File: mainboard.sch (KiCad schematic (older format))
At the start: 10 parts, among them J1 105017-1001, J2 XT60-M, U1 ESP32-WROOM-32E_(16MB), U2 CH340E, U3 AMS1117-3.3

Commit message: update
toevoegen mosfet en versterker in schematic
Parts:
- added C3, C4, C5, C6, C7, C8, C9: C, Capacitor_SMD:C_0805_2012Metric_Pad1.18x1.45mm_HandSolder, symbol Device:C
- added D1: D, Diode_SMD:D_0402_1005Metric_Pad0.77x0.64mm_HandSolder, symbol Device:D
- added Q1, Q2: AOD4184A, mylibs:DPAK228P994X240-4N, symbol AOD4184A:AOD4184A
- added R2, R3, R4, R5, R6: R, Resistor_SMD:R_0805_2012Metric_Pad1.20x1.40mm_HandSolder, symbol Device:R
- added U4: PAM8403DR, mylibs:SOIC127P605X150-16N, symbol PAM8403DR:PAM8403DR
- J1: symbol 105017-1001:105017-1001 -> mainboard-rescue:105017-1001-105017-1001
- J2: symbol XT60-M:XT60-M -> mainboard-rescue:XT60-M-XT60-M
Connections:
- net labels added: +OUT_L, +OUT_R, -OUT_L, -OUT_R, 5V, INL, INR, Mosfet_Out-, Mosfet_Trig, SHND, mute
- wire segments 20 -> 57
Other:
- note added: "High-Power-Mosfet\n"
- note added: "Programmer"
- note added: "Versterker-PAM8403 XH-M179\n"
- note added: "Voeding\n"
- moved on the sheet: C1, C2, R1, S1, S2, U1, U2, U3

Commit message: ik heb ervoor gezorgd dat de schakeling geen vuurwerk meer is
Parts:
- Q1, Q2: symbol AOD4184A:AOD4184A -> mainboard-rescue:AOD4184A-AOD4184A
- U4: symbol PAM8403DR:PAM8403DR -> mainboard-rescue:PAM8403DR-PAM8403DR
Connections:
- wire segments 57 -> 56
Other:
- moved on the sheet: C6
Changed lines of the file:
@@
 $EndComp
 $Comp
-L AOD4184A:AOD4184A Q1
+L mainboard-rescue:AOD4184A-AOD4184A Q1
 U 1 1 60421934
 P 9150 2900
@@
 	9700 3000 9700 3350
 $Comp
-L AOD4184A:AOD4184A Q2
+L mainboard-rescue:AOD4184A-AOD4184A Q2
 U 1 1 60422823
 P 9800 2900
@@
 L Device:C C6
 U 1 1 60534571
-P 4050 6100
-F 0 "C6" V 3798 6100 50  0000 C CNN
-F 1 "C" V 3889 6100 50  0000 C CNN
-F 2 "Capacitor_SMD:C_0805_2012Metric_Pad1.18x1.45mm_HandSolder" H 4088 5950 50  0001 C CNN
-F 3 "~" H 4050 6100 50  0001 C CNN
-	1    4050 6100
+P 4350 6100
+F 0 "C6" V 4098 6100 50  0000 C CNN
+F 1 "C" V 4189 6100 50  0000 C CNN
+F 2 "Capacitor_SMD:C_0805_2012Metric_Pad1.18x1.45mm_HandSolder" H 4388 5950 50  0001 C CNN
+F 3 "~" H 4350 6100 50  0001 C CNN
+	1    4350 6100
 	0    1    1    0
-$EndComp
-$Comp
-L power:GND #PWR0112
-U 1 1 605351B6
-P 4400 6100
-F 0 "#PWR0112" H 4400 5850 50  0001 C CNN
-F 1 "GND" V 4405 5972 50  0000 R CNN
-F 2 "" H 4400 6100 50  0001 C CNN
-F 3 "" H 4400 6100 50  0001 C CNN
-	1    4400 6100
-	0    -1   -1   0
 $EndComp
 Wire Notes Line
@@
 Versterker-PAM8403 XH-M179\n
 $Comp
-L PAM8403DR:PAM8403DR U4
+L mainboard-rescue:PAM8403DR-PAM8403DR U4
 U 1 1 60500031
 P 3300 6700
@@
 Text GLabel 1600 7400 3    50   Input ~ 0
 INL
-Wire Wire Line
-	4200 6100 4300 6100
 Text GLabel 4950 6200 2    50   Input ~ 0
 5V
 Wire Wire Line
-	4450 5950 4300 5950
-Wire Wire Line
-	4300 5950 4300 6100
-Connection ~ 4300 6100
-Wire Wire Line
-	4300 6100 4400 6100
-Wire Wire Line
 	4950 6200 4950 6300
-Text GLabel 4450 5950 2    50   Input ~ 0
-5V
 $Comp
 L power:GND #PWR0110
@@
 	1    0    0    -1
 $EndComp
+Text GLabel 4050 6000 1    50   Input ~ 0
+5V
+Wire Wire Line
+	3900 6100 4050 6100
+Wire Wire Line
+	4050 6100 4050 6000
+Connection ~ 4050 6100
+Wire Wire Line
+	4050 6100 4200 6100
+$Comp
+L power:GND #PWR?
+U 1 1 60477405
+P 4500 6100
+F 0 "#PWR?" H 4500 5850 50  0001 C CNN
+F 1 "GND" V 4505 5972 50  0000 R CNN
+F 2 "" H 4500 6100 50  0001 C CNN
+F 3 "" H 4500 6100 50  0001 C CNN
+	1    4500 6100
+	0    -1   -1   0
+$EndComp
 $EndSCHEMATC

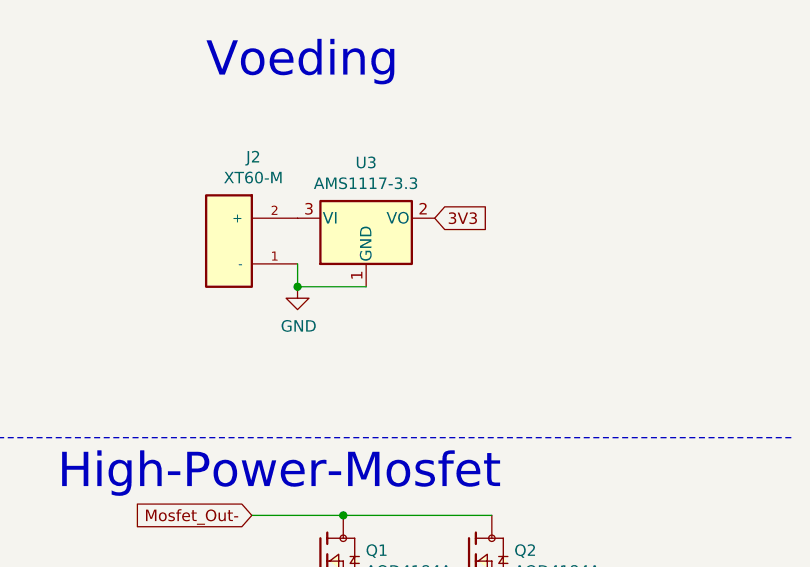
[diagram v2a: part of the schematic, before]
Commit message: condensator toegevoegd aan ldo
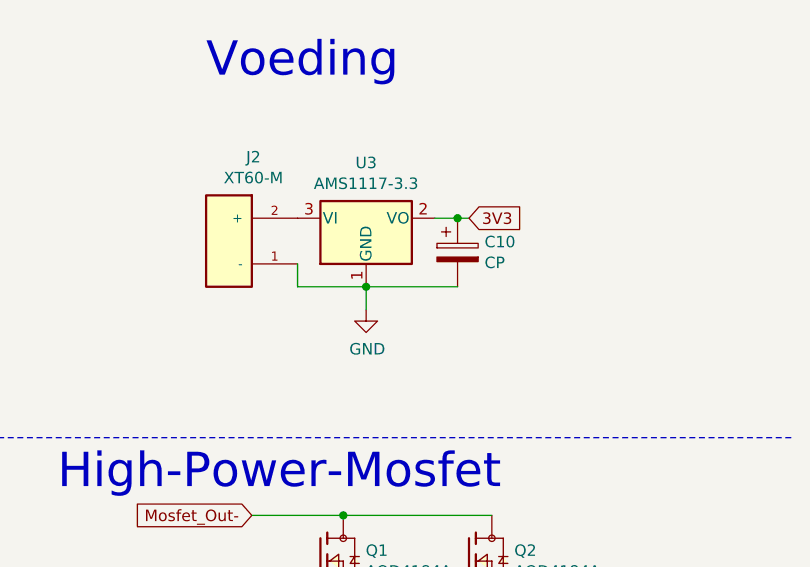
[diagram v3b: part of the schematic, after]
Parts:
- added C10: CP, Capacitor_Tantalum_SMD:CP_EIA-1608-08_AVX-J_Pad1.25x1.05mm_HandSolder, symbol Device:CP
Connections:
- wire segments 56 -> 60
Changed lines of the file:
@@
 Wire Wire Line
 	9250 2700 9900 2700
-Text GLabel 9650 1400 2    50   Input ~ 0
+Text GLabel 9800 1400 2    50   Input ~ 0
 3V3
-Connection ~ 9050 1700
 $Comp
 L power:GND #PWR01
 U 1 1 6046FD41
-P 9050 1700
-F 0 "#PWR01" H 9050 1450 50  0001 C CNN
-F 1 "GND" H 9055 1527 50  0000 C CNN
-F 2 "" H 9050 1700 50  0001 C CNN
-F 3 "" H 9050 1700 50  0001 C CNN
-	1    9050 1700
-	1    0    0    -1
-$EndComp
-Wire Wire Line
-	9050 1700 9050 1600
-Wire Wire Line
-	9350 1700 9050 1700
+P 9350 1800
+F 0 "#PWR01" H 9350 1550 50  0001 C CNN
+F 1 "GND" H 9355 1627 50  0000 C CNN
+F 2 "" H 9350 1800 50  0001 C CNN
+F 3 "" H 9350 1800 50  0001 C CNN
+	1    9350 1800
+	1    0    0    -1
+$EndComp
+Wire Wire Line
+	9350 1700 9350 1800
 $Comp
 L mainboard-rescue:XT60-M-XT60-M J2
@@
 	1    8750 1500
 	-1   0    0    1
-$EndComp
-$Comp
-L Regulator_Linear:AMS1117-3.3 U3
-U 1 1 60450E15
-P 9350 1400
-F 0 "U3" H 9350 1642 50  0000 C CNN
-F 1 "AMS1117-3.3" H 9350 1551 50  0000 C CNN
-F 2 "Package_TO_SOT_SMD:SOT-223-3_TabPin2" H 9350 1600 50  0001 C CNN
-F 3 "http://www.advanced-monolithic.com/pdf/ds1117.pdf" H 9450 1150 50  0001 C CNN
-	1    9350 1400
-	1    0    0    -1
 $EndComp
 Text GLabel 1900 1450 1    50   Input ~ 0
@@
 	4050 6100 4200 6100
 $Comp
-L power:GND #PWR?
+L power:GND #PWR04
 U 1 1 60477405
 P 4500 6100
-F 0 "#PWR?" H 4500 5850 50  0001 C CNN
+F 0 "#PWR04" H 4500 5850 50  0001 C CNN
 F 1 "GND" V 4505 5972 50  0000 R CNN
 F 2 "" H 4500 6100 50  0001 C CNN
@@
 	0    -1   -1   0
 $EndComp
+Wire Wire Line
+	9650 1400 9750 1400
+$Comp
+L Regulator_Linear:AMS1117-3.3 U3
+U 1 1 60450E15
+P 9350 1400
+F 0 "U3" H 9350 1642 50  0000 C CNN
+F 1 "AMS1117-3.3" H 9350 1551 50  0000 C CNN
+F 2 "Package_TO_SOT_SMD:SOT-223-3_TabPin2" H 9350 1600 50  0001 C CNN
+F 3 "http://www.advanced-monolithic.com/pdf/ds1117.pdf" H 9450 1150 50  0001 C CNN
+	1    9350 1400
+	1    0    0    -1
+$EndComp
+Wire Wire Line
+	9050 1600 9050 1700
+Wire Wire Line
+	9050 1700 9350 1700
+Connection ~ 9350 1700
+$Comp
+L Device:CP C10
+U 1 1 60484A4F
+P 9750 1550
+F 0 "C10" H 9868 1596 50  0000 L CNN
+F 1 "CP" H 9868 1505 50  0000 L CNN
+F 2 "Capacitor_Tantalum_SMD:CP_EIA-1608-08_AVX-J_Pad1.25x1.05mm_HandSolder" H 9788 1400 50  0001 C CNN
+F 3 "~" H 9750 1550 50  0001 C CNN
+	1    9750 1550
+	1    0    0    -1
+$EndComp
+Connection ~ 9750 1400
+Wire Wire Line
+	9750 1400 9800 1400
+Wire Wire Line
+	9750 1700 9350 1700
 $EndSCHEMATC

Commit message: ordenen pcb
kheb wa plek vrijgelaten voor de io pinnen
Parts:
- removed C2: C, Capacitor_SMD:C_0805_2012Metric_Pad1.18x1.45mm_HandSolder, symbol Device:C
- removed D1: D, Diode_SMD:D_0402_1005Metric_Pad0.77x0.64mm_HandSolder, symbol Device:D
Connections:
- wire segments 60 -> 57
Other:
- note added: "PWM\n"
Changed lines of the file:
@@
 	8850 5450 8850 5600
 Wire Wire Line
-	9100 5350 9100 4700
-Wire Wire Line
-	9100 4700 9550 4700
-Connection ~ 9550 4700
-Wire Wire Line
-	9550 4700 9650 4700
-Wire Wire Line
 	9650 4700 9650 5000
 Wire Wire Line
 	8850 5600 9250 5600
-$Comp
-L Device:C C2
-U 1 1 60436DBE
-P 9550 4850
-F 0 "C2" H 9665 4896 50  0000 L CNN
-F 1 "C" H 9665 4805 50  0000 L CNN
-F 2 "Capacitor_SMD:C_0805_2012Metric_Pad1.18x1.45mm_HandSolder" H 9588 4700 50  0001 C CNN
-F 3 "~" H 9550 4850 50  0001 C CNN
-	1    9550 4850
-	1    0    0    -1
-$EndComp
 $Comp
 L power:GND #PWR0103
@@
 Wire Wire Line
 	9250 5550 9250 5500
-Wire Wire Line
-	8350 5350 9100 5350
 NoConn ~ 10050 5500
 NoConn ~ 10050 6000
@@
 $EndComp
 $Comp
-L Device:D D1
-U 1 1 60426053
-P 9250 3900
-F 0 "D1" V 9296 3820 50  0000 R CNN
-F 1 "D" V 9205 3820 50  0000 R CNN
-F 2 "Diode_SMD:D_0402_1005Metric_Pad0.77x0.64mm_HandSolder" H 9250 3900 50  0001 C CNN
-F 3 "~" H 9250 3900 50  0001 C CNN
-	1    9250 3900
-	0    -1   -1   0
-$EndComp
-$Comp
 L Device:R R4
 U 1 1 604268D1
@@
 L power:GND #PWR0107
 U 1 1 6042DD5F
-P 9250 4050
-F 0 "#PWR0107" H 9250 3800 50  0001 C CNN
-F 1 "GND" H 9255 3877 50  0000 C CNN
-F 2 "" H 9250 4050 50  0001 C CNN
-F 3 "" H 9250 4050 50  0001 C CNN
-	1    9250 4050
+P 9250 3750
+F 0 "#PWR0107" H 9250 3500 50  0001 C CNN
+F 1 "GND" H 9255 3577 50  0000 C CNN
+F 2 "" H 9250 3750 50  0001 C CNN
+F 3 "" H 9250 3750 50  0001 C CNN
+	1    9250 3750
 	1    0    0    -1
 $EndComp
@@
 Wire Wire Line
 	9750 1700 9350 1700
+Wire Wire Line
+	9550 5000 9650 5000
+Connection ~ 9650 5000
+Text GLabel 9650 4700 2    50   Input ~ 0
+3V3
+Text GLabel 3950 1750 2    50   Input ~ 0
+3V3
+Text GLabel 3950 2050 2    50   Input ~ 0
+Mosfet_Trig
+Text Notes 3950 2650 0    50   ~ 0
+PWM\n
+Text Notes 3950 2750 0    50   ~ 0
+PWM\n
 $EndSCHEMATC

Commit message: sorry stef
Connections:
- net SHND: now also U1.14 (IO12)
- net mute: no longer names the net of U4.5 (MUTE)
- no-connect marks 4 -> 5
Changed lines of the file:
@@
 	1    0    0    -1
 $EndComp
-Text GLabel 2700 6400 0    50   Input ~ 0
-mute
 Connection ~ 4950 6650
 Wire Wire Line
@@
 Text Notes 3950 2750 0    50   ~ 0
 PWM\n
+NoConn ~ 2700 6400
+Text GLabel 3950 2350 2    50   Input ~ 0
+SHND
 $EndSCHEMATC

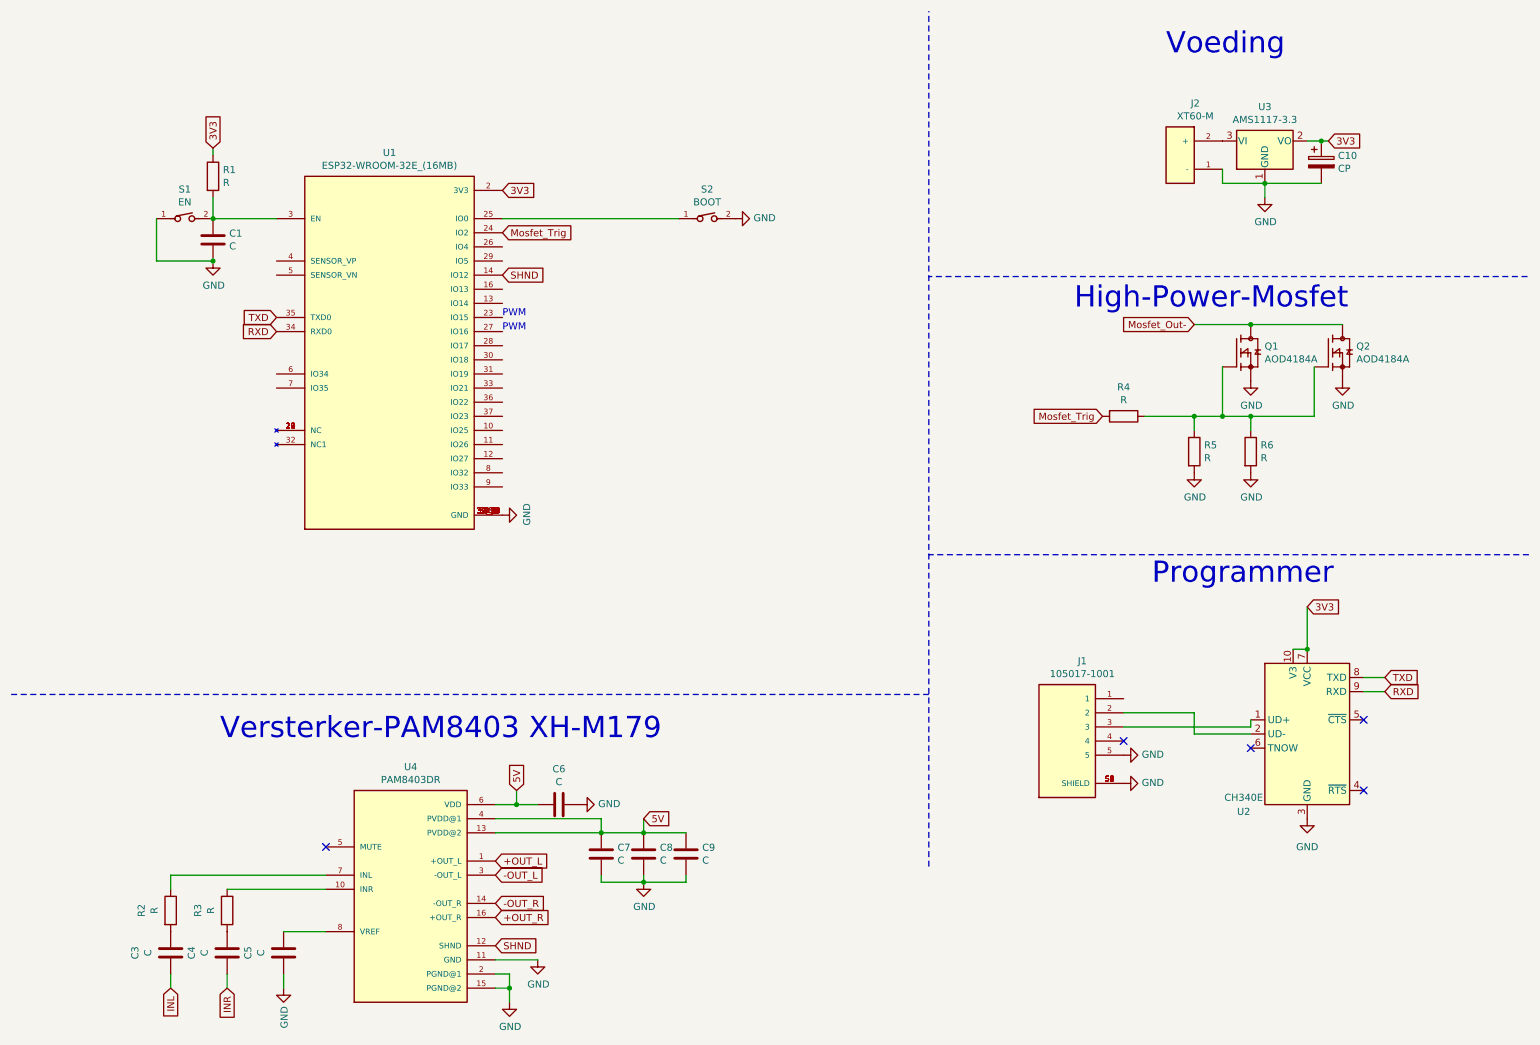
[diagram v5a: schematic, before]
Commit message: PCB herwerkt na feedback
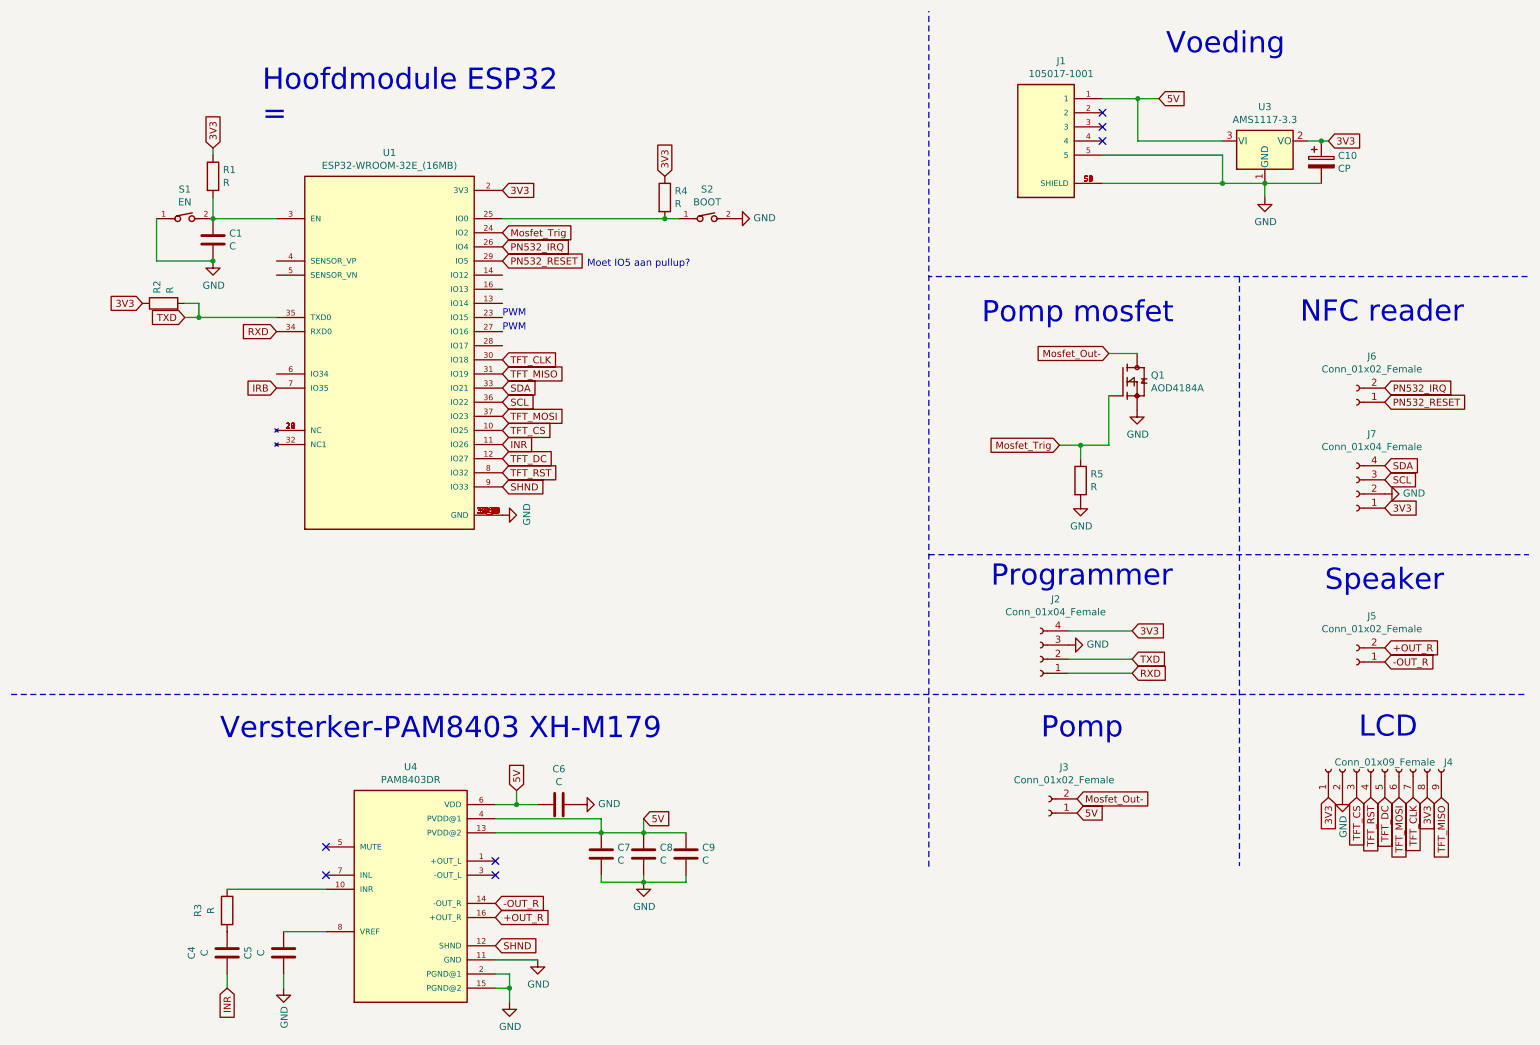
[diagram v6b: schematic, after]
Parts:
- removed C3: C, Capacitor_SMD:C_0805_2012Metric_Pad1.18x1.45mm_HandSolder, symbol Device:C
- removed J2: XT60-M, mylibs:AMASS_XT60-M, symbol mainboard-rescue:XT60-M-XT60-M
- removed Q2: AOD4184A, mylibs:DPAK228P994X240-4N, symbol mainboard-rescue:AOD4184A-AOD4184A
- removed R6: R, Resistor_SMD:R_0805_2012Metric_Pad1.20x1.40mm_HandSolder, symbol Device:R
- removed U2: CH340E, Package_SO:MSOP-10_3x3mm_P0.5mm, symbol Interface_USB:CH340E
- added J2: Conn_01x04_Female, Connector_PinSocket_2.54mm:PinSocket_1x04_P2.54mm_Vertical, symbol Connector:Conn_01x04_Female
- added J3, J5, J6: Conn_01x02_Female, Connector_PinSocket_2.54mm:PinSocket_1x02_P2.54mm_Vertical, symbol Connector:Conn_01x02_Female
- added J4: Conn_01x09_Female, Connector_PinSocket_2.54mm:PinSocket_1x09_P2.54mm_Vertical, symbol Connector:Conn_01x09_Female
- added J7: Conn_01x04_Female, symbol Connector:Conn_01x04_Female
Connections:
- net +OUT_R: now also J5.2 (Pin_2)
- net -OUT_R: now also J5.1 (Pin_1)
- net 3V3: now also R2.1, R4.1, J2.4 (Pin_4), J4.1 (Pin_1), J4.8 (Pin_8), J7.1 (Pin_1)
- net 5V: now also J1.1, U3.3 (VI), J3.1 (Pin_1)
- net GND: now also J2.3 (Pin_3), J4.2 (Pin_2), J7.2 (Pin_2)
- net INR: now also U1.11 (IO26)
- net Mosfet_Out-: now also J3.2 (Pin_2)
- net Mosfet_Trig: now also Q1.1, R5.1; no longer R4.2
- net RXD: now also J2.1 (Pin_1)
- net SHND: now also U1.9 (IO33); no longer U1.14 (IO12)
- net TXD: now also R2.2, J2.2 (Pin_2)
- net at S2.1, U1.25 (IO0): now also R4.2
- net TFT_CS: now reaches U1.10 (IO25)
- net TFT_CS: now also J4.3 (Pin_3)
- net TFT_DC: now reaches U1.12 (IO27)
- net TFT_DC: now also J4.5 (Pin_5)
- net PN532_IRQ: now reaches U1.26 (IO4)
- net PN532_IRQ: now also J6.2 (Pin_2)
- net PN532_RESET: now reaches U1.29 (IO5)
- net PN532_RESET: now also J6.1 (Pin_1)
- net TFT_CLK: now reaches U1.30 (IO18)
- net TFT_CLK: now also J4.7 (Pin_7)
- net TFT_MISO: now reaches U1.31 (IO19)
- net TFT_MISO: now also J4.9 (Pin_9)
- net SDA: now reaches U1.33 (IO21)
- net SDA: now also J7.4 (Pin_4)
- net SCL: now reaches U1.36 (IO22)
- net SCL: now also J7.3 (Pin_3)
- net TFT_MOSI: now reaches U1.37 (IO23)
- net TFT_MOSI: now also J4.6 (Pin_6)
- net IRB: now reaches U1.7 (IO35)
- net TFT_RST: now reaches U1.8 (IO32)
- net TFT_RST: now also J4.4 (Pin_4)
- net at U4.7 (INL): no longer R2.1
- net +OUT_L: no longer names the net of U4.1 (+OUT_L)
- net -OUT_L: no longer names the net of U4.3 (-OUT_L)
- no-connect marks 5 -> 7
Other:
- note added: "Hoofdmodule ESP32\n="
- note added: "LCD"
- note added: "Moet IO5 aan pullup?"
- note added: "NFC reader"
- note added: "Pomp"
- note added: "Pomp mosfet\n"
- note added: "Speaker\n"
- note removed: "High-Power-Mosfet\n"
- moved on the sheet: J1, Q1, R5

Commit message: tis fokking mooi wtf
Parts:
- removed C10: CP, Capacitor_Tantalum_SMD:CP_EIA-1608-08_AVX-J_Pad1.25x1.05mm_HandSolder, symbol Device:CP
- added C2: 100n, Capacitor_SMD:C_0805_2012Metric_Pad1.18x1.45mm_HandSolder, symbol Device:C
- added C3: 22u, Capacitor_SMD:C_0805_2012Metric_Pad1.18x1.45mm_HandSolder, symbol Device:C
- added R6, R7: 10K, Resistor_SMD:R_0805_2012Metric_Pad1.20x1.40mm_HandSolder, symbol Device:R
- C1: value C -> 100n
- C4: value C -> 0.47u
- C5: value C -> 0.1u
- C6, C7, C9: value C -> 1u
- C8: value C -> 470u
- J7: footprint (none) -> Connector_PinSocket_2.54mm:PinSocket_1x02_P2.54mm_Vertical
- R1, R2, R3, R4, R5: value R -> 10K
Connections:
- net 3V3: now also J4.9 (Pin_9), C2.2, C3.1, R6.2; no longer J4.8 (Pin_8)
- net 5V: now also C6.1; no longer C6.2
- net GND: now also C6.2, C2.1, C3.2, R7.1; no longer C6.1
- net PN532_RESET: now also R6.1
- net SHND: now also R7.2
- net TFT_CLK: now also J4.8 (Pin_8); no longer J4.7 (Pin_7)
- net TFT_CS: now also J4.4 (Pin_4); no longer J4.3 (Pin_3)
- net TFT_MISO: now also J4.7 (Pin_7); no longer J4.9 (Pin_9)
- net TFT_RST: now also J4.3 (Pin_3); no longer J4.4 (Pin_4)
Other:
- moved on the sheet: C6, C9, R4
